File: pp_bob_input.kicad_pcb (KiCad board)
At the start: 2 copper layers, 98.8 x 72.1 mm, 22 parts, among them P1 2X8, P2 2X5, P3 2X4, P4 13X2, U1 74LVC245, U2 74LVC245, U3 74LS541

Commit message: Commit V0.2
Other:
- board text added: "BBB CNC PORT 2 13 LINE INPUT 4 LINE OUTPUT INTERFACE REV 0.2"
- board text removed: "BBB CNC PORT 2 13 LINE INPUT 4 LINE OUTPUT INTERFACE REV 0.1"
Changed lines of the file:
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@@
     (links 95)
     (no_connects 1)
-    (area 25.387299 25.387299 124.218701 97.548701)
+    (area 25.387299 24.1874 124.460001 98.675)
     (thickness 1.6)
     (drawings 49)
@@
     (effects (font (size 1.016 1.016) (thickness 0.2032)))
   )
-  (gr_text "BBB CNC PORT 2\n13 LINE INPUT  \n4 LINE OUTPUT\nINTERFACE REV 0.1" (at 116.586 57.15 90) (layer F.SilkS)
+  (gr_text "BBB CNC PORT 2\n13 LINE INPUT  \n4 LINE OUTPUT\nINTERFACE REV 0.2" (at 116.586 57.15 90) (layer F.SilkS)
     (effects (font (size 1.27 1.27) (thickness 0.254)) (justify left))
   )

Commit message: Redraw layout
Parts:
- removed P1: 2X8, w_conn_strip:vasch_strip_8x2
- removed P2: 2X5, w_conn_strip:vasch_strip_5x2
- removed P3: 2X4, w_conn_strip:vasch_strip_4x2
- removed the REF** at (120.2, 73.4)
- removed the REF** at (29.4, 73.4)
- added J_IN_1: ST_1x04, w_conn_pt-1,5:pt_1,5-4-3,5-h, F.Cu at (48.1, 31.8)
- added J_IN_2: ST_1x04, w_conn_pt-1,5:pt_1,5-4-3,5-h, F.Cu at (65.9, 31.8)
- added J_IN_3: ST_1x04, w_conn_pt-1,5:pt_1,5-4-3,5-h, F.Cu at (83.7, 31.8)
- added J_IN_4: ST_1x04, w_conn_pt-1,5:pt_1,5-4-3,5-h, F.Cu at (101.5, 31.8)
- added J_IN_5: ST_1x12, w_conn_pt-1,5:pt_1,5-15-3,5-h, F.Cu at (117.5, 61.5)
- added J_OUT_2: ST_1x12, w_conn_pt-1,5:pt_1,5-12-3,5-h, F.Cu at (74.8, 91.4)
- added REF**: R_Array_SIP9, Resistors_THT:R_Array_SIP9, F.Cu at (108.6, 70.5)
- added REF**: R_Array_SIP9, Resistors_THT:R_Array_SIP9, F.Cu at (79.4, 40.6)
- added REF**: R_Array_SIP5, Resistors_THT:R_Array_SIP5, F.Cu at (56.5, 82.5)
- moved R1 194.8 mm to (234.9, 94.6)
- moved PPWRIN_1 156.5 mm to (259.1, 57.1)
- moved PPWRSEL_1 156.5 mm to (247.0, 62.2)
- moved RN1 156.5 mm to (237.5, 61.0)
- moved PCE_1 155.6 mm to (188.0, 73.0)
- moved C1 54.6 mm to (48.9, 45.7), turned to 270 degrees
- moved U1 42.0 mm to (54.0, 53.3), turned to 90 degrees
- moved C3 39.2 mm to (87.0, 77.5), turned to 90 degrees
- moved U3 36.5 mm to (81.9, 69.8), turned to 270 degrees
- moved RN2 29.0 mm to (90.8, 67.9)
- moved U2 29.0 mm to (95.9, 45.1)
- moved C2 29.0 mm to (103.5, 40.0)
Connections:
- PPWRIN_1 pad 5: Net-(PPWRIN_1-Pad5) -> (no net)
- RN1 pad 1: GND -> Net-(J_IN_5-Pad12)
- U3 pad 11: Net-(U3-Pad11) -> /OUT-17
- U3 pad 12: Net-(U3-Pad12) -> /OUT-16
- U3 pad 13: Net-(U3-Pad13) -> /OUT-14
- U3 pad 14: Net-(U3-Pad14) -> /OUT-01
- U3 pad 15: /OUT-17 -> (no net)
- U3 pad 16: /OUT-16 -> (no net)
- U3 pad 17: /OUT-14 -> (no net)
- U3 pad 18: /OUT-01 -> (no net)
- U3 pad 2: DB_01 -> Net-(U3-Pad2)
- U3 pad 3: DB_14 -> Net-(U3-Pad2)
- U3 pad 4: DB_16 -> Net-(U3-Pad2)
- U3 pad 5: DB_17 -> Net-(U3-Pad2)
- U3 pad 6: GND -> DB_01
- U3 pad 7: GND -> DB_14
- U3 pad 8: GND -> DB_16
- U3 pad 9: GND -> DB_17
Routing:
- net CHIP_ENABLE: track 191.6 -> 0.00 mm
- net +5V: track 69.4 -> 0.00 mm
- net /OUT-17: track 56.4 -> 13.3 mm
- net /IN-05: track 55.2 -> 14.3 mm
- net /IN-04: track 53.9 -> 13.9 mm
- net DB_10: track 47.6 -> 82.9 mm
- net /OUT-16: track 55.2 -> 19.9 mm
- net /IN-11: track 49.2 -> 14.0 mm
- net DB_11: track 52.3 -> 84.6 mm
- net /IN-12: track 50.1 -> 17.9 mm
- net DB_02: track 74.2 -> 42.3 mm
- net /IN-07: track 57.7 -> 26.3 mm
- net /IN-06: track 56.4 -> 25.1 mm
- net DB_03: track 78.9 -> 47.9 mm
- net DB_04: track 77.5 -> 47.4 mm
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- removed copper zone on F.Cu, net +3V3
- removed copper zone on F.Cu, net +5V
- removed copper zone on B.Cu, net GND

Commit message: Schematic still to update, PCB about 95% done
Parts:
- removed PCE_1: 1X4, Pin_Headers:Pin_Header_Straight_1x04_Pitch2.54mm
- removed the RN1 at (237.5, 61.0)
- added SEL_1: Pin_Header_Straight_1x03_Pitch2.54mm, Pin_Headers:Pin_Header_Straight_1x03_Pitch2.54mm, F.Cu at (84.5, 45.7)
- added SEL_2: Pin_Header_Straight_1x03_Pitch2.54mm, Pin_Headers:Pin_Header_Straight_1x03_Pitch2.54mm, F.Cu at (108.6, 85.1)
- added SEL_3: Pin_Header_Straight_1x03_Pitch2.54mm, Pin_Headers:Pin_Header_Straight_1x03_Pitch2.54mm, F.Cu at (101.0, 85.1)
- moved PPWRIN_1 231.7 mm to (29.2, 86.4), turned to 180 degrees
- moved PPWRSEL_1 206.0 mm to (41.9, 81.9), turned to 180 degrees
- moved R1 185.9 mm to (49.5, 81.9), turned to 90 degrees
- moved RN4 12.7 mm to (69.2, 82.5), turned to 180 degrees
- renumbered REF** to RN1, REF** to RN3, REF** to RN4
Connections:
- P4 pad 26: /SCHP -> CHIP_ENABLE
- RN4 pad 2: /OUT-17 -> /OUT-01
- RN4 pad 3: /OUT-16 -> /OUT-14
- RN4 pad 4: /OUT-14 -> /OUT-16
- RN4 pad 5: /OUT-01 -> /OUT-17
- U3 pad 2: Net-(U3-Pad2) -> GND
- U3 pad 3: Net-(U3-Pad2) -> GND
- U3 pad 4: Net-(U3-Pad2) -> GND
- U3 pad 5: Net-(U3-Pad2) -> GND
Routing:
- net +3V3: track 0.00 -> 184.0 mm
- net CHIP_ENABLE: track 0.00 -> 159.9 mm
- net GND: track 0.00 -> 20.9 mm
- net /IN-12: track 17.9 -> 34.1 mm
- net /VDD_+5v: track 0.00 -> 13.5 mm
- net /SYS_+5v: track 0.00 -> 13.0 mm
- net /OUT-01: track 30.4 -> 35.4 mm
- net +5V: track 0.00 -> 5.08 mm
- net /IN-08: track 37.8 -> 36.8 mm
- added copper zone on F.Cu, net +5V
- added copper zone on B.Cu, net GND
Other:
- board text added: "16"
- board text added: "PD"
- board text added: "PU"
- board text removed: "3V3 LOGIC ONLY"
- board text removed: "CE"
- board text removed: "PWR SELECT"
- board text removed: "SCHP"

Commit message: Initial V0.3 commit
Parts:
- added G***: LOGO, w_logo:Logo_silk_warning_5x4.2mm, F.Cu at (105.4, 92.7)
- added G***: LOGO, w_logo:Logo_silk_OSHW_12x13mm, F.Cu at (55.2, 60.3)
- added G***: LOGO, w_logo:Logo_silk_warning_5x4.2mm, F.Cu at (39.4, 52.7)
- added SEL_2: 1X3, Pin_Headers:Pin_Header_Straight_1x03_Pitch2.54mm, F.Cu at (102.2, 80.6)
- J_IN_5: value ST_1x12 -> ST_1x15
- RN1, RN3: value R_Array_SIP9 -> 4k7
- RN2: value 10k -> 3k3
- RN4: value R_Array_SIP5 -> 4k7
- SEL_1: value Pin_Header_Straight_1x03_Pitch2.54mm -> 1X3
- SEL_3: renamed from SEL_2; value Pin_Header_Straight_1x03_Pitch2.54mm -> 1X3
- SEL_4: renamed from SEL_3; value Pin_Header_Straight_1x03_Pitch2.54mm -> 1X3
- moved SEL_4 54.7 mm to (46.4, 82.5), turned to 90 degrees
- moved R1 13.9 mm to (43.8, 69.2), turned to 180 degrees
- moved RN4 12.7 mm to (56.5, 82.5), turned to 0 degrees
- moved PWRIN_1 11.4 mm to (29.2, 74.9), turned to 0 degrees
- moved SEL_1 8.08 mm to (90.2, 40.0), turned to 270 degrees
- moved PWRSEL_1 5.12 mm to (39.4, 77.5), turned to 0 degrees
- moved SEL_3 4.45 mm to (108.6, 80.6)
- moved U1 0.64 mm to (54.0, 52.7)
- moved C1 0.63 mm to (48.9, 45.1)
- moved RN1 0.63 mm to (79.4, 40.0)
- renumbered PPWRIN_1 to PWRIN_1, PPWRSEL_1 to PWRSEL_1
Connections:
- RN1 pad 1: (no net) -> Net-(RN1-Pad1)
- RN2 pad 1: GND -> Net-(RN2-Pad1)
- RN3 pad 1: (no net) -> Net-(RN3-Pad1)
- RN4 pad 1: (no net) -> Net-(RN4-Pad1)
- RN4 pad 2: /OUT-01 -> /OUT-17
- RN4 pad 3: /OUT-14 -> /OUT-16
- RN4 pad 4: /OUT-16 -> /OUT-14
- RN4 pad 5: /OUT-17 -> /OUT-01
- SEL_1 pad 2: (no net) -> Net-(RN1-Pad1)
- SEL_3 pad 2: (no net) -> Net-(RN3-Pad1)
- SEL_4 pad 2: (no net) -> Net-(RN4-Pad1)
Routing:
- net Net-(RN2-Pad1): track 0.00 -> 20.8 mm
- net Net-(RN4-Pad1): track 0.00 -> 12.5 mm
- net Net-(RN1-Pad1): track 0.00 -> 11.8 mm
- net Net-(RN3-Pad1): track 0.00 -> 11.2 mm
- net +3V3: track 184.0 -> 178.0 mm
- net /VDD_+5v: track 13.5 -> 10.2 mm
- net /SYS_+5v: track 13.0 -> 11.2 mm
- net /IN-07: track 26.3 -> 25.0 mm
- net /IN-06: track 25.1 -> 23.9 mm
- net /IN-05: track 14.3 -> 13.0 mm
- net /IN-04: track 13.9 -> 12.7 mm
- net /IN-10: track 20.4 -> 21.5 mm
- net /IN-09: track 38.0 -> 37.0 mm
- net DB_15: track 79.8 -> 78.9 mm
- net DB_12: track 80.5 -> 79.6 mm
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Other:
- board text added: "5V SEL"
- board text added: "BBB CNC PORT 2 13 LINE INPUT 4 LINE OUTPUT INTERFACE REV 0.3"
- board text added: "SET BOTH IN SAME POSITION"
- board text added: "SYS"
- board text added: "VDD"
- board text removed: "BBB CNC PORT 2 13 LINE INPUT 4 LINE OUTPUT INTERFACE REV 0.2"
- board text removed: "SYS_+5v"
- board text removed: "VDD_+5v"

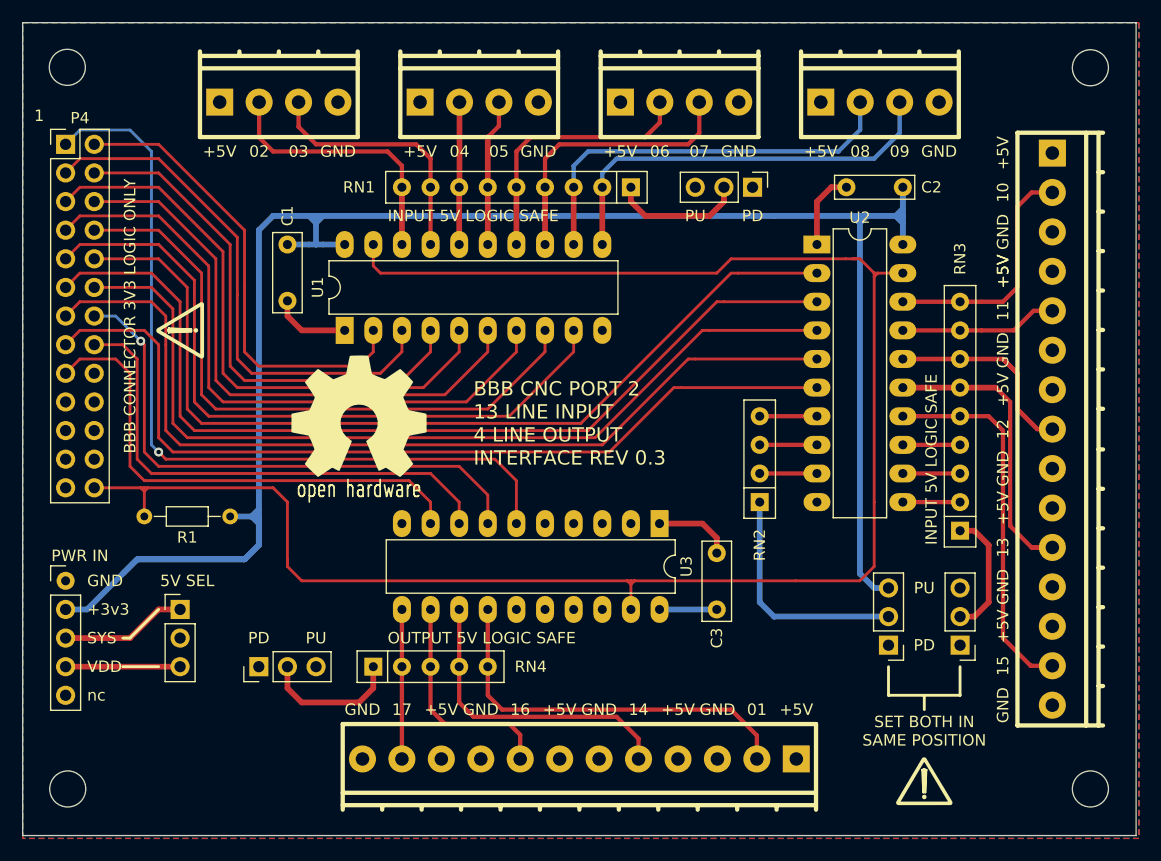
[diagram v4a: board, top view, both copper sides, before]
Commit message: Clean up in line with pp_bob_output_v0.3
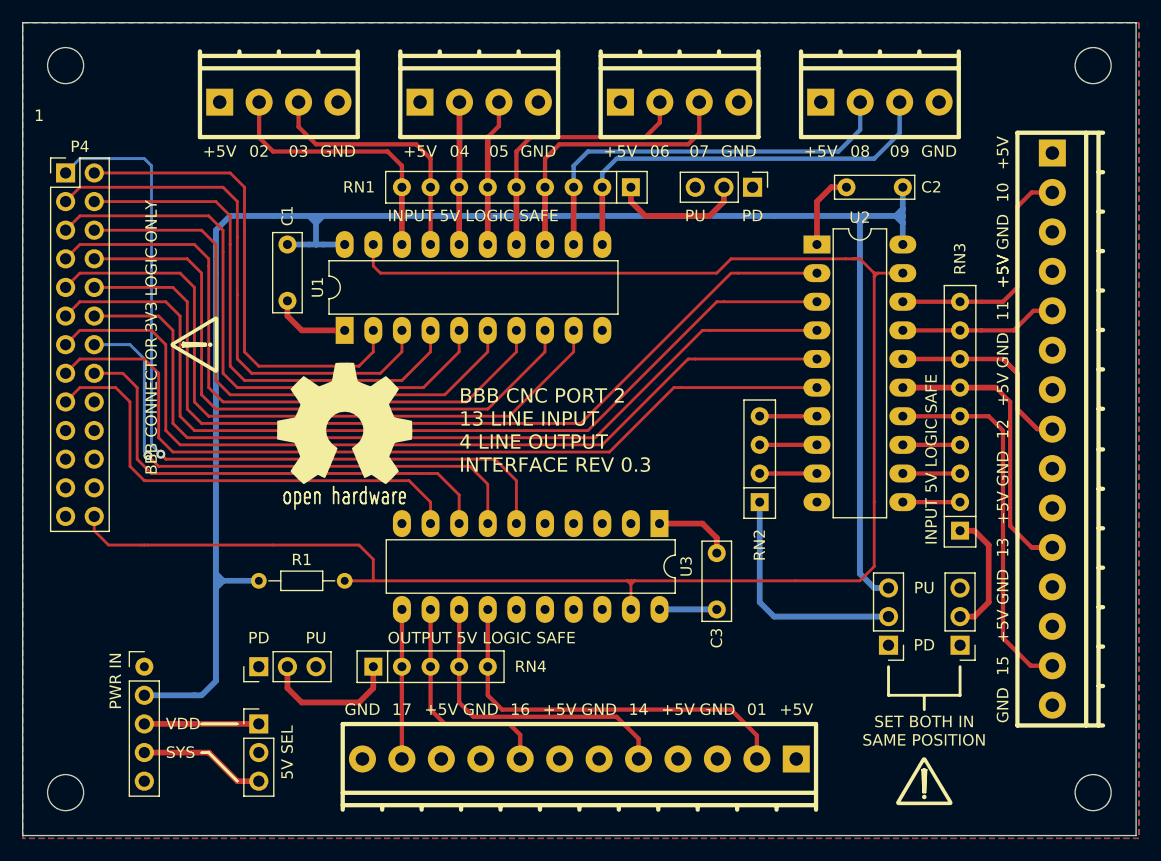
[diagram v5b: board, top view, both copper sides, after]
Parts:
- moved PWRSEL_1 12.3 mm to (46.4, 87.6)
- moved PWRIN_1 10.3 mm to (36.2, 82.5)
- moved R1 6.25 mm to (46.4, 74.9), turned to 0 degrees
- moved P4 2.54 mm to (29.2, 38.7)
- moved G*** 1.80 mm to (40.6, 54.0)
- moved G*** 1.42 mm to (54.0, 61.0)
- moved REF** 0.41 mm to (120.4, 93.7)
- moved REF** 0.38 mm to (29.2, 93.7)
- moved REF** 0.31 mm to (120.4, 29.2)
- moved REF** 0.22 mm to (29.2, 29.2)
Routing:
- net +3V3: track 178.0 -> 167.2 mm
- net CHIP_ENABLE: track 160.1 -> 156.6 mm
- net DB_17: track 44.9 -> 42.4 mm
- net DB_15: track 78.9 -> 76.3 mm
- net DB_13: track 81.6 -> 79.0 mm
- net DB_16: track 45.3 -> 43.1 mm
- net DB_12: track 79.6 -> 77.4 mm
- net DB_10: track 82.0 -> 80.2 mm
- net DB_01: track 73.1 -> 71.3 mm
- net DB_11: track 83.7 -> 81.9 mm
- net DB_09: track 62.5 -> 61.1 mm
- net DB_14: track 49.6 -> 48.4 mm
- net DB_02: track 41.7 -> 42.9 mm
- net /SYS_+5v: track 11.2 -> 10.2 mm
- net DB_08: track 56.9 -> 55.9 mm
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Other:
- board text removed: "+3v3"
- board text removed: "nc"

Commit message: Layout modded to max output board
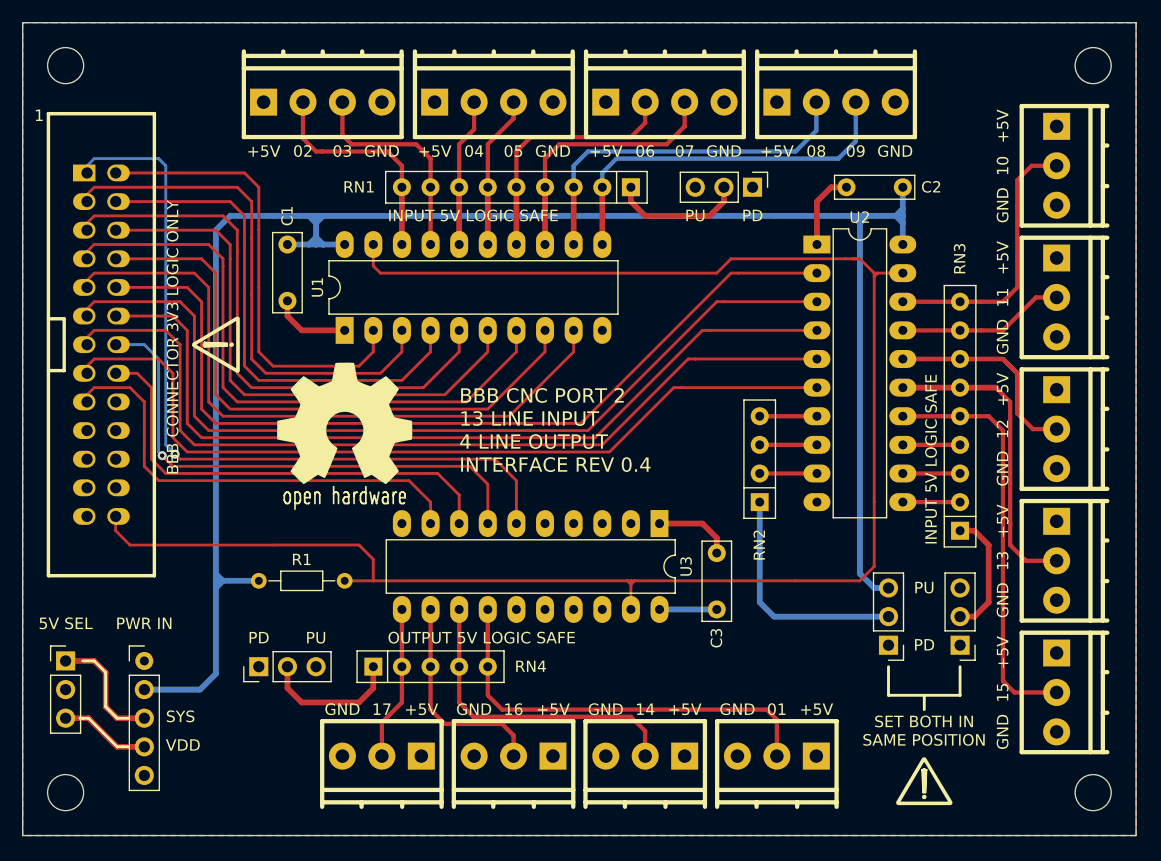
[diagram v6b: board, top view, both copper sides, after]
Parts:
- removed J_OUT_2: ST_1x12, w_conn_pt-1,5:pt_1,5-12-3,5-h
- added J_IN_6: ST_1x03, w_conn_pt-1,5:pt_1,5-3-3,5-h, F.Cu at (117.9, 49.8)
- added J_IN_7: ST_1x03, w_conn_pt-1,5:pt_1,5-3-3,5-h, F.Cu at (117.9, 61.5)
- added J_IN_8: ST_1x03, w_conn_pt-1,5:pt_1,5-3-3,5-h, F.Cu at (117.9, 73.2)
- added J_IN_9: ST_1x03, w_conn_pt-1,5:pt_1,5-3-3,5-h, F.Cu at (117.9, 84.8)
- added J_OUT_5: ST_1x03, w_conn_pt-1,5:pt_1,5-3-3,5-h, F.Cu at (92.3, 91.2)
- added J_OUT_6: ST_1x03, w_conn_pt-1,5:pt_1,5-3-3,5-h, F.Cu at (80.6, 91.2)
- added J_OUT_7: ST_1x03, w_conn_pt-1,5:pt_1,5-3-3,5-h, F.Cu at (69.0, 91.2)
- added J_OUT_8: ST_1x03, w_conn_pt-1,5:pt_1,5-3-3,5-h, F.Cu at (57.3, 91.2)
- J_IN_5: value ST_1x15 -> ST_1x03; footprint w_conn_pt-1,5:pt_1,5-15-3,5-h -> w_conn_pt-1,5:pt_1,5-3-3,5-h
- P4: footprint Pin_Headers:Pin_Header_Straight_2x13_Pitch2.54mm -> w_conn_strip:vasch_strip_13x2
- moved J_IN_5 23.4 mm to (117.9, 38.1)
- moved PWRSEL_1 18.0 mm to (29.2, 82.0)
- moved P4 15.6 mm to (32.4, 54.0), turned to 270 degrees
- moved J_IN_1 3.89 mm to (52.0, 31.8)
- moved J_IN_4 3.89 mm to (97.6, 31.8)
- moved G*** 1.91 mm to (42.5, 54.0)
- moved J_IN_2 1.30 mm to (67.2, 31.8)
- moved J_IN_3 1.30 mm to (82.4, 31.8)
- moved PWRIN_1 0.51 mm to (36.2, 82.0)
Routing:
- net /IN-02: track 24.5 -> 20.6 mm
- net /IN-08: track 36.2 -> 32.3 mm
- net /IN-15: track 33.2 -> 36.8 mm
- net /IN-03: track 22.7 -> 19.2 mm
- net /IN-09: track 37.0 -> 33.5 mm
- net /VDD_+5v: track 11.2 -> 8.04 mm
- net /IN-10: track 21.5 -> 24.2 mm
- net /OUT-01: track 35.1 -> 37.4 mm
- net DB_01: track 71.3 -> 69.2 mm
- net CHIP_ENABLE: track 156.6 -> 154.4 mm
- net /IN-12: track 34.1 -> 32.2 mm
- net /IN-07: track 25.0 -> 23.3 mm
- net DB_17: track 42.4 -> 40.8 mm
- net DB_07: track 56.8 -> 55.2 mm
- net DB_13: track 79.0 -> 77.5 mm
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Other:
- board text added: "BBB CNC PORT 2 13 LINE INPUT 4 LINE OUTPUT INTERFACE REV 0.4"
- board text removed: "BBB CNC PORT 2 13 LINE INPUT 4 LINE OUTPUT INTERFACE REV 0.3"
